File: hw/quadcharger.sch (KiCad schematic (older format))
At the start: 4 parts, among them J2 Conn_01x08, U2 MCP23017_SS, U5 4052

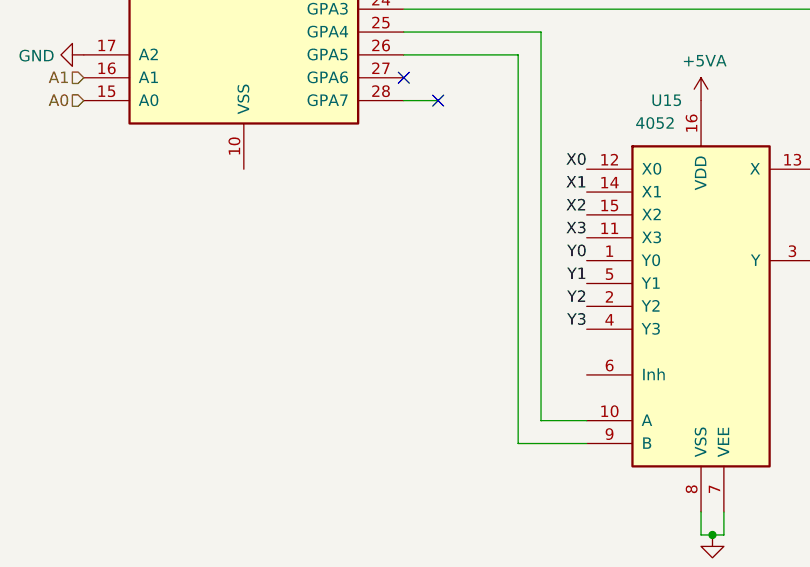
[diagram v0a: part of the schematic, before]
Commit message: fix mux enable pin, reroute some traces
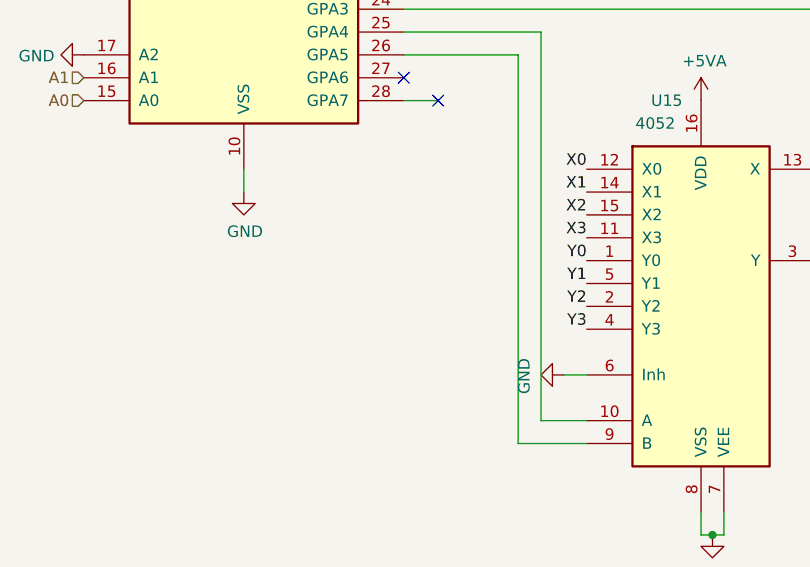
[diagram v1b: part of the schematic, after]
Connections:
- net GND: now also U2.10 (VSS), U5.6 (Inh)
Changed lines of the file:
@@
 EESchema Schematic File Version 4
-LIBS:charger2-cache
 EELAYER 30 0
 EELAYER END
@@
 	1    0    0    -1
 $EndComp
+$Comp
+L power:GND #PWR0154
+U 1 1 5DC8DD5E
+P 5000 5150
+AR Path="/5DC82B0A/5DC8DD5E" Ref="#PWR0154"  Part="1"
+AR Path="/5DC581CC/5DC8DD5E" Ref="#PWR0111"  Part="1"
+F 0 "#PWR0154" H 5000 4900 50  0001 C CNN
+F 1 "GND" H 5005 4977 50  0000 C CNN
+F 2 "" H 5000 5150 50  0001 C CNN
+F 3 "" H 5000 5150 50  0001 C CNN
+	1    5000 5150
+	0    1    1    0
+$EndComp
+Wire Wire Line
+	5000 5150 5100 5150
+$Comp
+L power:GND #PWR?
+U 1 1 5DCA0DAA
+P 3600 4350
+AR Path="/5DC82B0A/5DCA0DAA" Ref="#PWR?"  Part="1"
+AR Path="/5DC581CC/5DCA0DAA" Ref="#PWR?"  Part="1"
+F 0 "#PWR?" H 3600 4100 50  0001 C CNN
+F 1 "GND" H 3605 4177 50  0000 C CNN
+F 2 "" H 3600 4350 50  0001 C CNN
+F 3 "" H 3600 4350 50  0001 C CNN
+	1    3600 4350
+	1    0    0    -1
+$EndComp
+Wire Wire Line
+	3600 4350 3600 4250
 $EndSCHEMATC
